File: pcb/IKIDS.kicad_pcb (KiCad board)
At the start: 2 copper layers, 142.9 x 95.3 mm, 25 parts, among them U1 Elite-C

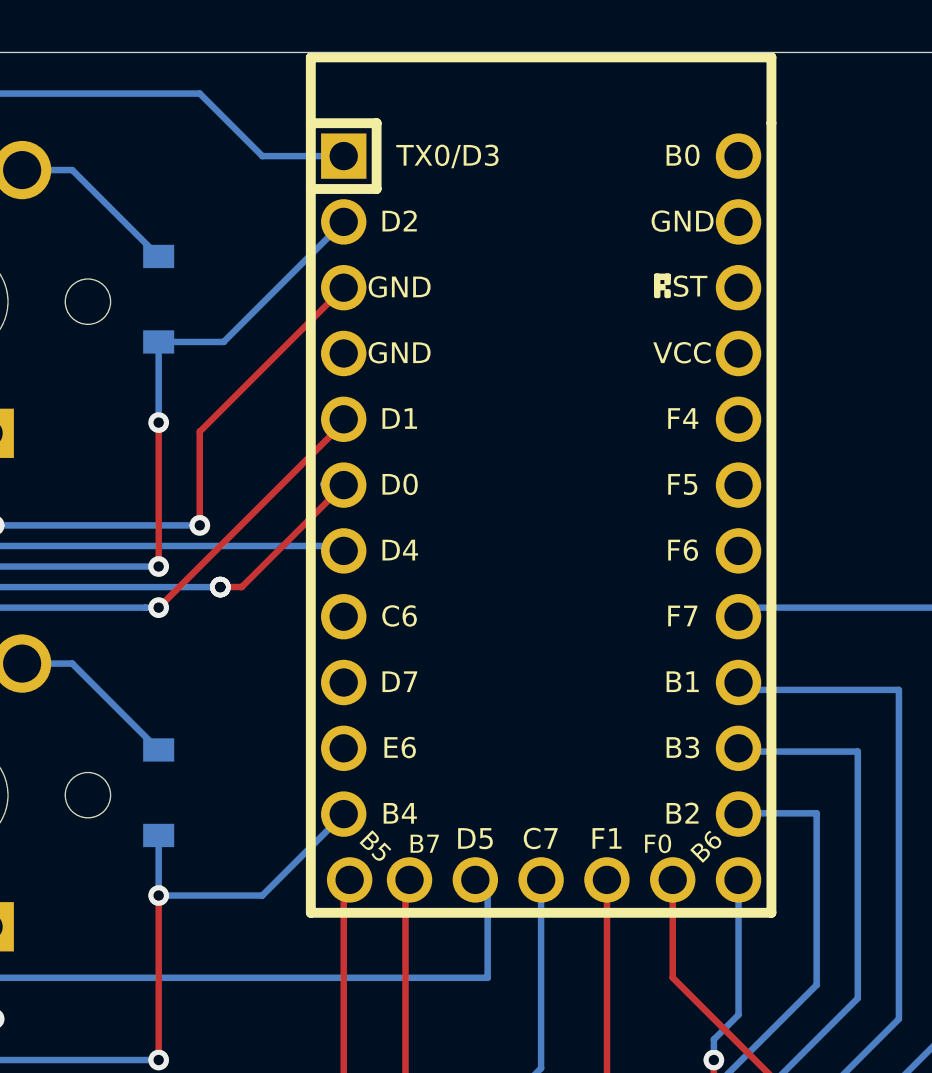
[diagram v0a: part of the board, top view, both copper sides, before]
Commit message: Flipped Elite-c for easier case making.
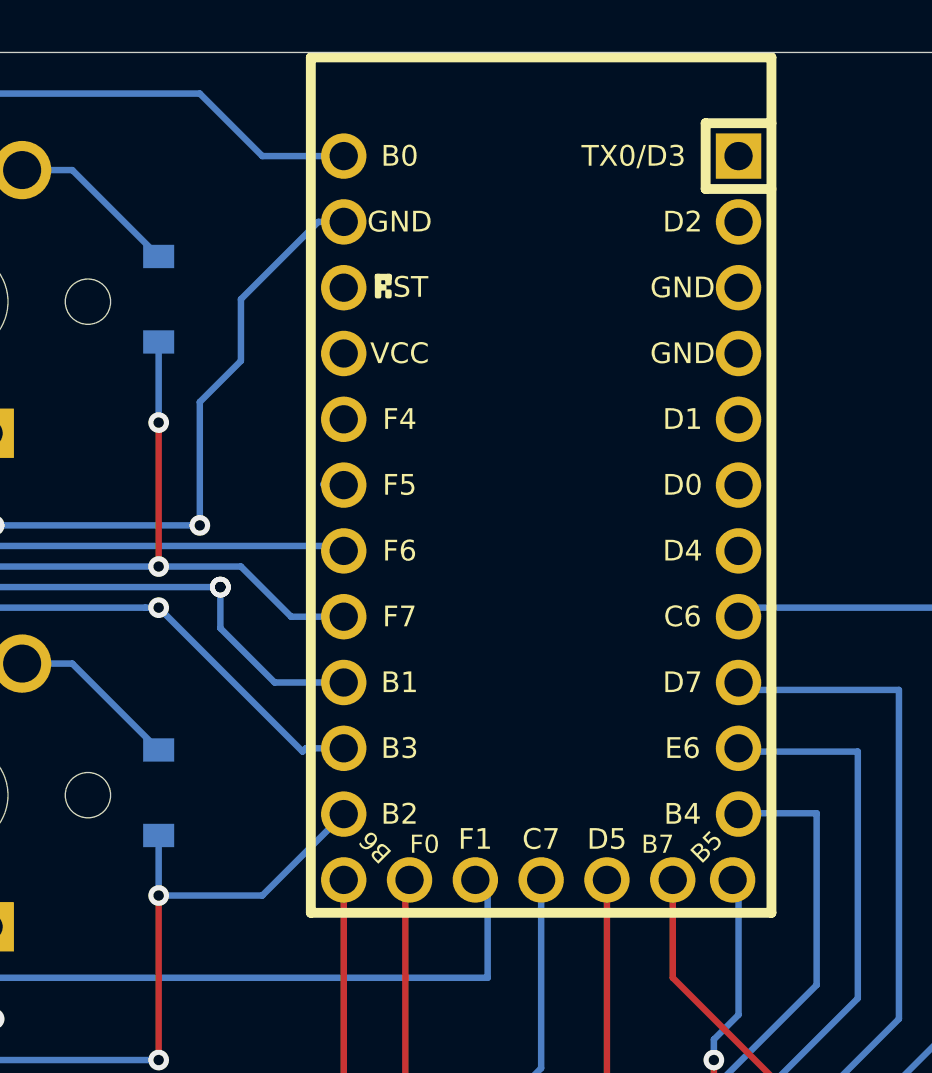
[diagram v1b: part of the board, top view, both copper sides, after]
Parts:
- U1: moved to B.Cu
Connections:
- U1 pad 1: col1 -> Net-(U1-Pad1)
- U1 pad 10: Net-(U1-Pad10) -> led7
- U1 pad 11: row2 -> led9
- U1 pad 12: row3 -> row4
- U1 pad 13: row4 -> row3
- U1 pad 14: led9 -> row2
- U1 pad 15: led7 -> led1
- U1 pad 16: led8 -> led2
- U1 pad 17: row5 -> row1
- U1 pad 18: Net-(U1-Pad18) -> led3
- U1 pad 2: row1 -> Net-(U1-Pad2)
- U1 pad 23: Net-(U1-Pad23) -> gnd
- U1 pad 24: Net-(U1-Pad24) -> col1
- U1 pad 25: col2 -> col3
- U1 pad 26: led4 -> led6
- U1 pad 28: led6 -> led4
- U1 pad 29: col3 -> col2
- U1 pad 3: gnd -> Net-(U1-Pad3)
- U1 pad 5: led1 -> Net-(U1-Pad5)
- U1 pad 6: led2 -> Net-(U1-Pad6)
- U1 pad 7: led3 -> Net-(U1-Pad7)
- U1 pad 8: Net-(U1-Pad8) -> row5
- U1 pad 9: Net-(U1-Pad9) -> led8
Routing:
- net gnd: track 237.9 -> 241.0 mm
- net Net-(U1-Pad19): track 0.00 -> 0.81 mm
- net led1: track 63.9 -> 63.2 mm
